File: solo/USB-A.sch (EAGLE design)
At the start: 26 parts, among them U1 USB_TRACES

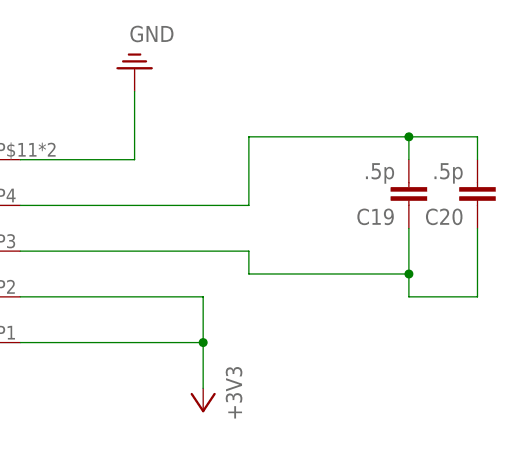
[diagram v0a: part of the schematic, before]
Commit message: update cap values
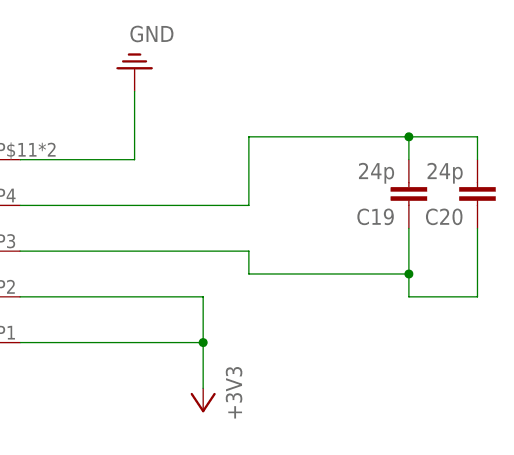
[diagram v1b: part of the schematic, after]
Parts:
- C19, C20: value .5p -> 24p
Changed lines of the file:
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@@
 <part name="SUPPLY16" library="supply2" library_urn="urn:adsk.eagle:library:372" deviceset="PE" device="" value="GND"/>
 <part name="+3V16" library="supply1" library_urn="urn:adsk.eagle:library:371" deviceset="+3V3" device=""/>
-<part name="C19" library="efm-fido" library_urn="urn:adsk.eagle:library:4245354" deviceset="CAPACITOR" device="" package3d_urn="urn:adsk.eagle:package:4245806/9" value=".5p"/>
-<part name="C20" library="efm-fido" library_urn="urn:adsk.eagle:library:4245354" deviceset="CAPACITOR" device="" package3d_urn="urn:adsk.eagle:package:4245806/9" value=".5p"/>
+<part name="C19" library="efm-fido" library_urn="urn:adsk.eagle:library:4245354" deviceset="CAPACITOR" device="" package3d_urn="urn:adsk.eagle:package:4245806/9" value="24p"/>
+<part name="C20" library="efm-fido" library_urn="urn:adsk.eagle:library:4245354" deviceset="CAPACITOR" device="" package3d_urn="urn:adsk.eagle:package:4245806/9" value="24p"/>
 <part name="C3" library="efm-fido" library_urn="urn:adsk.eagle:library:4245354" deviceset="CAPACITOR" device="" package3d_urn="urn:adsk.eagle:package:4245806/9" value="4.7u"/>
 <part name="C7" library="efm-fido" library_urn="urn:adsk.eagle:library:4245354" deviceset="CAPACITOR" device="" package3d_urn="urn:adsk.eagle:package:4245806/9" value="4.7u"/>
